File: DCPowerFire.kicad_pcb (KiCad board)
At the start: 4 copper layers, 51.7 x 7.9 mm, 49 parts, among them J1 Conn_01x01, J10 Conn_01x01, J11 Conn_01x01, J2 Conn_01x01, J3 USB_B_Micro, J4 Conn_01x01, J5 Conn_01x01, J6 Conn_02x03_Odd_Even, J7 Conn_01x01, J8 Conn_01x01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

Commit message: migrate project to current KiCad nightly
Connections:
- U3 pad 49: GND -> (no net)
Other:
- net class Default removed

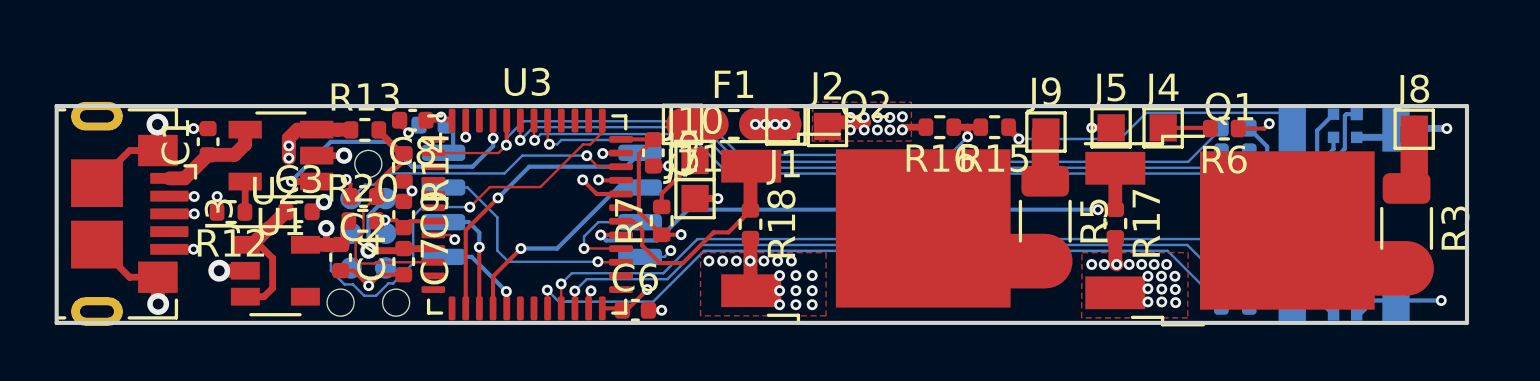
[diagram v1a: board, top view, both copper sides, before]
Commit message: finish USB ID trace and fix DRC errors
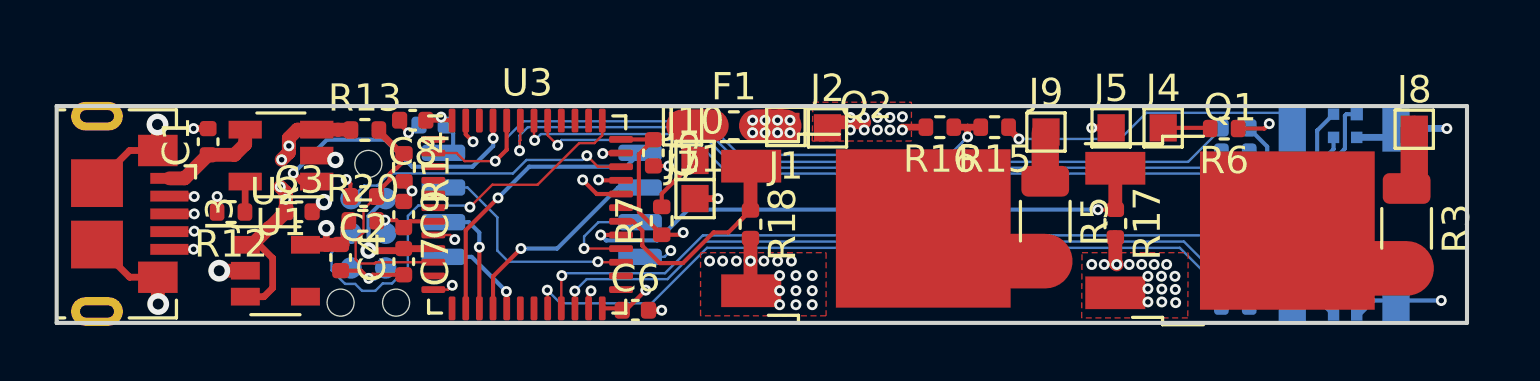
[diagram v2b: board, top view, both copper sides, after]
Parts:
- moved J1 0.05 mm to (106.7, 52.8)
- moved F1 0.05 mm to (104.8, 52.8)
- moved J2 0.05 mm to (108.2, 52.9)
- moved J7 0.05 mm to (102.9, 52.8)
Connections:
- J3 pad 4: Net-(J3-Pad4) -> USB_ID
- J6 pad 6: Net-(J6-Pad6) -> unconnected-(J6-Pad6)
- U2 pad 4: Net-(U2-Pad4) -> unconnected-(U2-Pad4)
- U3 pad 1: Net-(U3-Pad1) -> unconnected-(U3-Pad1)
- U3 pad 11: Net-(U3-Pad11) -> unconnected-(U3-Pad11)
- U3 pad 12: Net-(U3-Pad12) -> USB_ID
- U3 pad 13: Net-(U3-Pad13) -> unconnected-(U3-Pad13)
- U3 pad 18: Net-(U3-Pad18) -> unconnected-(U3-Pad18)
- U3 pad 19: Net-(U3-Pad19) -> unconnected-(U3-Pad19)
- U3 pad 25: Net-(U3-Pad25) -> unconnected-(U3-Pad25)
- U3 pad 26: Net-(U3-Pad26) -> unconnected-(U3-Pad26)
- U3 pad 3: Net-(U3-Pad3) -> unconnected-(U3-Pad3)
- U3 pad 31: Net-(U3-Pad31) -> unconnected-(U3-Pad31)
- U3 pad 38: Net-(U3-Pad38) -> unconnected-(U3-Pad38)
- U3 pad 4: Net-(U3-Pad4) -> unconnected-(U3-Pad4)
- U3 pad 40: Net-(U3-Pad40) -> unconnected-(U3-Pad40)
- U3 pad 46: Net-(U3-Pad46) -> unconnected-(U3-Pad46)
- U3 pad 5: Net-(U3-Pad5) -> unconnected-(U3-Pad5)
- U3 pad 6: Net-(U3-Pad6) -> unconnected-(U3-Pad6)
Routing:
- net USB_ID: track 0.00 -> 11.9 mm, vias 0 -> 2
- net +BATT: track 9.67 -> 10.8 mm, vias 6 -> 12
- net Net-(R15-Pad2): track 23.5 -> 24.6 mm
- net G_1: track 27.8 -> 28.7 mm
- net USB_DN: track 19.9 -> 20.4 mm
- net USB_DP: track 19.4 -> 20.0 mm

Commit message: add missing NTC connections & begin silkscreen
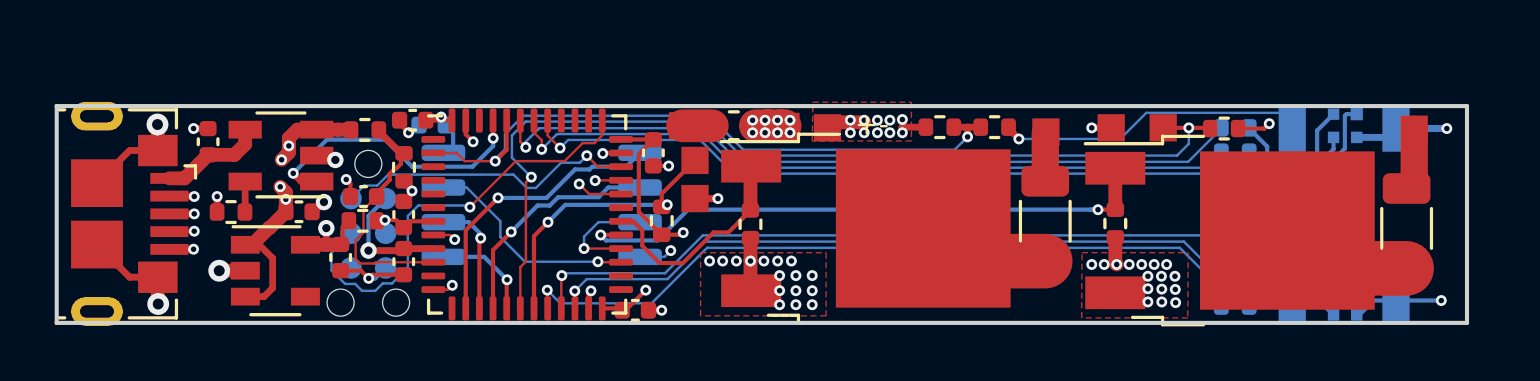
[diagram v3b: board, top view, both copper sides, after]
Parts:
- J1: value Conn_01x01 -> Coil+; footprint TestPoint:TestPoint_Pad_1.0x1.0mm -> LeoDJ-kicad:TestPoint_Pad_1.0x1.0mm_NoSilk
- J10: value Conn_01x01 -> NTC2_SIG; footprint TestPoint:TestPoint_Pad_1.0x1.0mm -> LeoDJ-kicad:TestPoint_Pad_1.0x1.0mm_NoSilk
- J11: value Conn_01x01 -> NTC2_GND; footprint TestPoint:TestPoint_Pad_1.0x1.0mm -> LeoDJ-kicad:TestPoint_Pad_1.0x1.0mm_NoSilk
- J2: value Conn_01x01 -> BAT-; footprint TestPoint:TestPoint_Pad_1.0x1.0mm -> LeoDJ-kicad:TestPoint_Pad_1.0x1.0mm_NoSilk
- J4: value Conn_01x01 -> NTC1_SIG; footprint TestPoint:TestPoint_Pad_1.0x1.0mm -> LeoDJ-kicad:TestPoint_Pad_1.0x1.0mm_NoSilk
- J5: value Conn_01x01 -> NTC1_GND; footprint TestPoint:TestPoint_Pad_1.0x1.0mm -> LeoDJ-kicad:TestPoint_Pad_1.0x1.0mm_NoSilk
- J7: value Conn_01x01 -> BAT+; footprint TestPoint:TestPoint_Pad_1.0x1.0mm -> LeoDJ-kicad:TestPoint_Pad_1.0x1.0mm_NoSilk
- J8: value Conn_01x01 -> Coil_1; footprint TestPoint:TestPoint_Pad_1.0x1.0mm -> LeoDJ-kicad:TestPoint_Pad_1.0x1.0mm_NoSilk
- J9: value Conn_01x01 -> Coil_2; footprint TestPoint:TestPoint_Pad_1.0x1.0mm -> LeoDJ-kicad:TestPoint_Pad_1.0x1.0mm_NoSilk
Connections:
- J10 pad 1: Net-(J10-Pad1) -> NTC2
- J4 pad 1: Net-(J4-Pad1) -> NTC1
- R6 pad 2: Net-(J4-Pad1) -> NTC1
- R7 pad 2: Net-(J10-Pad1) -> NTC2
- U3 pad 18: unconnected-(U3-Pad18) -> NTC1
- U3 pad 19: unconnected-(U3-Pad19) -> NTC2
- U3 pad 39: SW_Safty -> unconnected-(U3-Pad39)
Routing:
- net NTC1: track 0.00 -> 34.8 mm, vias 0 -> 2
- net NTC2: track 0.00 -> 10.4 mm, vias 0 -> 2
- net Net-(J10-Pad1): track 2.20 -> 0.00 mm
- net Net-(J4-Pad1): track 1.74 -> 0.00 mm
- net G_1: track 28.7 -> 28.1 mm
- net MISO: track 7.90 -> 8.47 mm
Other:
- board text added: "+-"

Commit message: add solder pad silkscreen
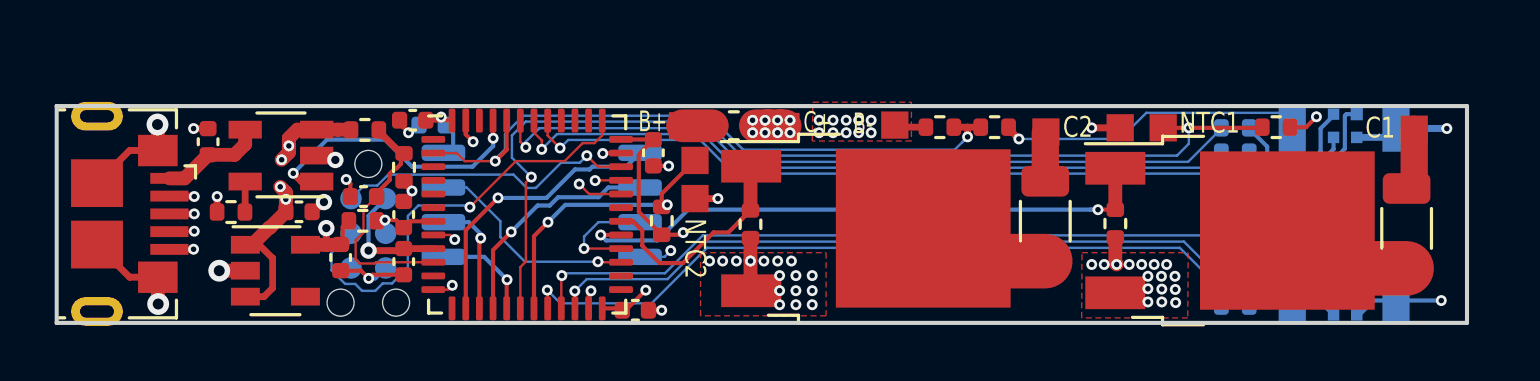
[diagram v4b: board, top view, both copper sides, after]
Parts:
- moved J2 2.47 mm to (110.7, 52.8), turned to 180 degrees
- moved R6 1.91 mm to (124.7, 52.8)
- moved J5 0.33 mm to (118.9, 52.9)
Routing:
- net NTC1: track 34.8 -> 36.7 mm
- net GND: track 29.8 -> 28.9 mm
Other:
- board text added: "B+"
- board text added: "B-"
- board text added: "C+"
- board text added: "C1"
- board text added: "C2"
- board text added: "NTC1"
- board text added: "NTC2"
- board text removed: "+-"

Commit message: bottom silkscreen
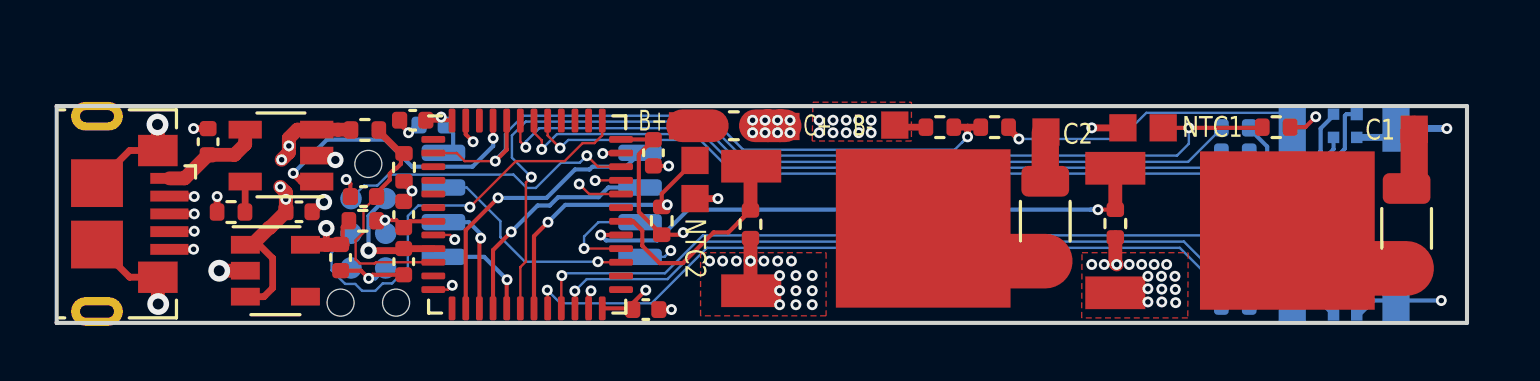
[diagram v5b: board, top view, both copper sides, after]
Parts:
- moved C6 0.38 mm to (101.6, 59.5)
- moved J5 0.10 mm to (119.0, 52.9)

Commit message: add lid switch pads
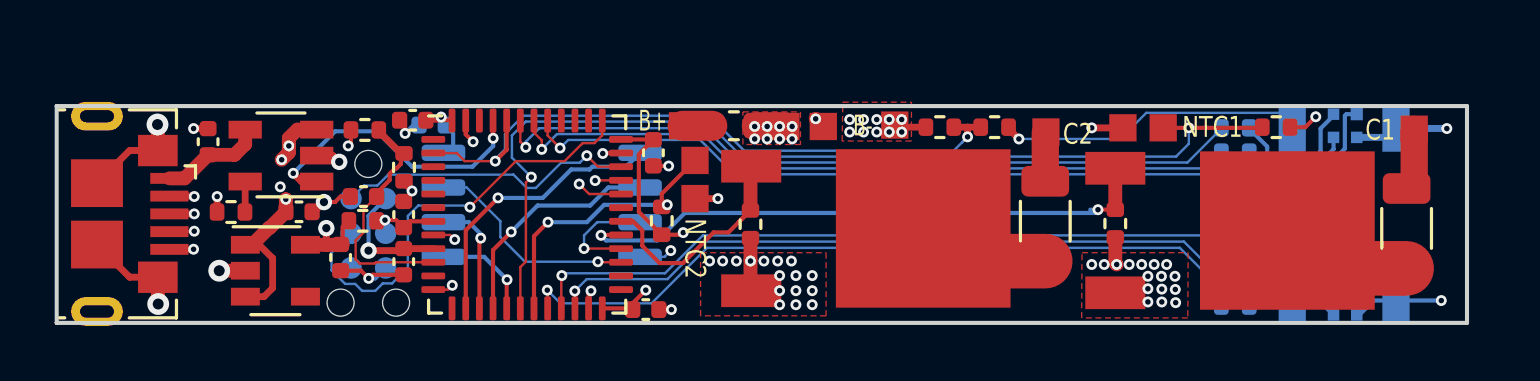
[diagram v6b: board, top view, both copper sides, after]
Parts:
- added J12: SafetySwitch, LeoDJ-kicad:TestPoint_Pad_1.0x1.0mm_NoSilk, F.Cu at (108.1, 52.8)
- J1: value Coil+ -> Coil+/SafetySwitch
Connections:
- net Net-(F1-Pad1) renamed /+BATT_RAW
- F1 pad 2: +BATT -> +BATT_FUSED
- J1 pad 1: +BATT -> +BATT_FUSED
- U1 pad 3: +BATT -> +BATT_FUSED
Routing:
- net +BATT: track 10.8 -> 31.0 mm, vias 12 -> 4
- net +BATT_FUSED: track 0.00 -> 3.18 mm, vias 0 -> 10
- net GND: track 29.0 -> 29.9 mm, vias 63 -> 62
- added copper zone on F.Cu, net +BATT_FUSED
- added copper zone on In1.Cu, net +BATT_FUSED
- removed copper zone on In1.Cu, net +BATT
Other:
- board text removed: "C+"

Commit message: add title text
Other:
- board text added: "MIDI Arc Lighter v1.0"
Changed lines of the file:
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@@
       (outputformat 1)
       (mirror false)
-      (drillshape 1)
+      (drillshape 0)
       (scaleselection 1)
-      (outputdirectory "")
+      (outputdirectory "gerber/")
     )
   )
@@
     (fp_line (start 3.5 -3.5) (end 3.5 3.5) (layer "F.Fab") (width 0.1))
     (fp_line (start -3.5 3.5) (end -3.5 -2.5) (layer "F.Fab") (width 0.1))
-    (pad "" smd roundrect locked (at -0.7 2.1) (size 1.13 1.13) (layers "F.Paste") (roundrect_rratio 0.221239))
-    (pad "" smd roundrect locked (at -2.1 -0.7) (size 1.13 1.13) (layers "F.Paste") (roundrect_rratio 0.221239))
-    (pad "" smd roundrect locked (at -2.1 -2.1) (size 1.13 1.13) (layers "F.Paste") (roundrect_rratio 0.221239))
-    (pad "" smd roundrect locked (at 0.7 -0.7) (size 1.13 1.13) (layers "F.Paste") (roundrect_rratio 0.221239))
-    (pad "" smd roundrect locked (at 0.7 0.7) (size 1.13 1.13) (layers "F.Paste") (roundrect_rratio 0.221239))
-    (pad "" smd roundrect locked (at 0.7 -2.1) (size 1.13 1.13) (layers "F.Paste") (roundrect_rratio 0.221239))
-    (pad "" smd roundrect locked (at 2.1 -0.7) (size 1.13 1.13) (layers "F.Paste") (roundrect_rratio 0.221239))
-    (pad "" smd roundrect locked (at 0.7 2.1) (size 1.13 1.13) (layers "F.Paste") (roundrect_rratio 0.221239))
-    (pad "" smd roundrect locked (at 2.1 0.7) (size 1.13 1.13) (layers "F.Paste") (roundrect_rratio 0.221239))
-    (pad "" smd roundrect locked (at -2.1 2.1) (size 1.13 1.13) (layers "F.Paste") (roundrect_rratio 0.221239))
-    (pad "" smd roundrect locked (at -0.7 -2.1) (size 1.13 1.13) (layers "F.Paste") (roundrect_rratio 0.221239))
-    (pad "" smd roundrect locked (at -0.7 0.7) (size 1.13 1.13) (layers "F.Paste") (roundrect_rratio 0.221239))
-    (pad "" smd roundrect locked (at -0.7 -0.7) (size 1.13 1.13) (layers "F.Paste") (roundrect_rratio 0.221239))
-    (pad "" smd roundrect locked (at -2.1 0.7) (size 1.13 1.13) (layers "F.Paste") (roundrect_rratio 0.221239))
-    (pad "" smd roundrect locked (at 2.1 -2.1) (size 1.13 1.13) (layers "F.Paste") (roundrect_rratio 0.221239))
-    (pad "" smd roundrect locked (at 2.1 2.1) (size 1.13 1.13) (layers "F.Paste") (roundrect_rratio 0.221239))
+    (pad "" smd roundrect locked (at -0.7 2.1) (size 1.13 1.13) (layers "F.Paste") (roundrect_rratio 0.2212389381))
+    (pad "" smd roundrect locked (at -2.1 -0.7) (size 1.13 1.13) (layers "F.Paste") (roundrect_rratio 0.2212389381))
+    (pad "" smd roundrect locked (at -2.1 -2.1) (size 1.13 1.13) (layers "F.Paste") (roundrect_rratio 0.2212389381))
+    (pad "" smd roundrect locked (at 0.7 -0.7) (size 1.13 1.13) (layers "F.Paste") (roundrect_rratio 0.2212389381))
+    (pad "" smd roundrect locked (at 0.7 0.7) (size 1.13 1.13) (layers "F.Paste") (roundrect_rratio 0.2212389381))
+    (pad "" smd roundrect locked (at 0.7 -2.1) (size 1.13 1.13) (layers "F.Paste") (roundrect_rratio 0.2212389381))
+    (pad "" smd roundrect locked (at 2.1 -0.7) (size 1.13 1.13) (layers "F.Paste") (roundrect_rratio 0.2212389381))
+    (pad "" smd roundrect locked (at 0.7 2.1) (size 1.13 1.13) (layers "F.Paste") (roundrect_rratio 0.2212389381))
+    (pad "" smd roundrect locked (at 2.1 0.7) (size 1.13 1.13) (layers "F.Paste") (roundrect_rratio 0.2212389381))
+    (pad "" smd roundrect locked (at -2.1 2.1) (size 1.13 1.13) (layers "F.Paste") (roundrect_rratio 0.2212389381))
+    (pad "" smd roundrect locked (at -0.7 -2.1) (size 1.13 1.13) (layers "F.Paste") (roundrect_rratio 0.2212389381))
+    (pad "" smd roundrect locked (at -0.7 0.7) (size 1.13 1.13) (layers "F.Paste") (roundrect_rratio 0.2212389381))
+    (pad "" smd roundrect locked (at -0.7 -0.7) (size 1.13 1.13) (layers "F.Paste") (roundrect_rratio 0.2212389381))
+    (pad "" smd roundrect locked (at -2.1 0.7) (size 1.13 1.13) (layers "F.Paste") (roundrect_rratio 0.2212389381))
+    (pad "" smd roundrect locked (at 2.1 -2.1) (size 1.13 1.13) (layers "F.Paste") (roundrect_rratio 0.2212389381))
+    (pad "" smd roundrect locked (at 2.1 2.1) (size 1.13 1.13) (layers "F.Paste") (roundrect_rratio 0.2212389381))
     (pad "1" smd roundrect locked (at -3.4375 -2.75) (size 0.875 0.25) (layers "F.Cu" "F.Paste" "F.Mask") (roundrect_rratio 0.25)
       (net 53 "unconnected-(U3-Pad1)") (pinfunction "VBAT") (pintype "power_in"))
@@
     (fp_line (start -1.6 0.8) (end -1.6 -0.8) (layer "F.Fab") (width 0.1))
     (fp_line (start -1.6 -0.8) (end 1.6 -0.8) (layer "F.Fab") (width 0.1))
-    (pad "1" smd roundrect locked (at -1.4625 0 270) (size 1.125 1.75) (layers "F.Cu" "F.Paste" "F.Mask") (roundrect_rratio 0.222222)
+    (pad "1" smd roundrect locked (at -1.4625 0 270) (size 1.125 1.75) (layers "F.Cu" "F.Paste" "F.Mask") (roundrect_rratio 0.2222222222)
       (net 20 "Net-(J8-Pad1)") (pintype "passive"))
-    (pad "2" smd roundrect locked (at 1.4625 0 270) (size 1.125 1.75) (layers "F.Cu" "F.Paste" "F.Mask") (roundrect_rratio 0.222222)
+    (pad "2" smd roundrect locked (at 1.4625 0 270) (size 1.125 1.75) (layers "F.Cu" "F.Paste" "F.Mask") (roundrect_rratio 0.2222222222)
       (net 46 "Net-(Q1-Pad2)") (pintype "passive"))
     (model "${KISYS3DMOD}/Resistor_SMD.3dshapes/R_1206_3216Metric.wrl"
@@
     (fp_line (start 1.6 -0.8) (end 1.6 0.8) (layer "F.Fab") (width 0.1))
     (fp_line (start -1.6 -0.8) (end 1.6 -0.8) (layer "F.Fab") (width 0.1))
-    (pad "1" smd roundrect locked (at -1.4625 0 270) (size 1.125 1.75) (layers "F.Cu" "F.Paste" "F.Mask") (roundrect_rratio 0.222222)
+    (pad "1" smd roundrect locked (at -1.4625 0 270) (size 1.125 1.75) (layers "F.Cu" "F.Paste" "F.Mask") (roundrect_rratio 0.2222222222)
       (net 21 "Net-(J9-Pad1)") (pintype "passive"))
-    (pad "2" smd roundrect locked (at 1.4625 0 270) (size 1.125 1.75) (layers "F.Cu" "F.Paste" "F.Mask") (roundrect_rratio 0.222222)
+    (pad "2" smd roundrect locked (at 1.4625 0 270) (size 1.125 1.75) (layers "F.Cu" "F.Paste" "F.Mask") (roundrect_rratio 0.2222222222)
       (net 47 "Net-(Q2-Pad2)") (pintype "passive"))
     (model "${KISYS3DMOD}/Resistor_SMD.3dshapes/R_1206_3216Metric.wrl"
@@
   (gr_line (start 131.65 60) (end 131.65 52.06) (layer "Edge.Cuts") (width 0.15))
   (gr_line (start 80 60) (end 80 52.06) (layer "Edge.Cuts") (width 0.15))
+  (gr_text "MIDI Arc Lighter v1.0" (at 111.633 55.5498) (layer "B.SilkS")
+    (effects (font (size 1 1) (thickness 0.15)) (justify mirror))
+  )
   (gr_text "B+" (at 101.8286 52.6034) (layer "F.SilkS")
     (effects (font (size 0.762 0.5) (thickness 0.125)))
@@
     (polygon
       (pts
-        (xy 133.4008 65.4812)
-        (xy 77.089 65.913)
-        (xy 77.3684 46.9392)
-        (xy 132.9944 46.9392)      )
+        (xy 132.2324 60.6044)
+        (xy 79.7052 60.2742)
+        (xy 79.4512 51.308)
+        (xy 132.1308 51.6382)      )
     )
   )
@@
     (polygon
       (pts
-        (xy 140.1064 69.3166)
-        (xy 74.4474 69.6214)
-        (xy 80.01 52.07)
-        (xy 132.9944 44.0182)      )
-    )
-  )
+        (xy 133.161619 61.08734)
+        (xy 78.8162 61.1378)
+        (xy 78.8162 50.800403)
+        (xy 133.186173 50.775173)      )
+    )
+  )

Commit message: generate fabrication outputs
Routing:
- net GND: vias 62 -> 65
